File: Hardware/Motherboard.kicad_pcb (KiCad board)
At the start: 2 copper layers, 11 parts, among them J1 Pin_Header_02x08, J2 Pin_Header_02x08, J3 Pin_Header_02x08, U1 PIC18F26K22-I-SO, U2 FT240XS, U3 TXB0104D, U4 TXB0104D

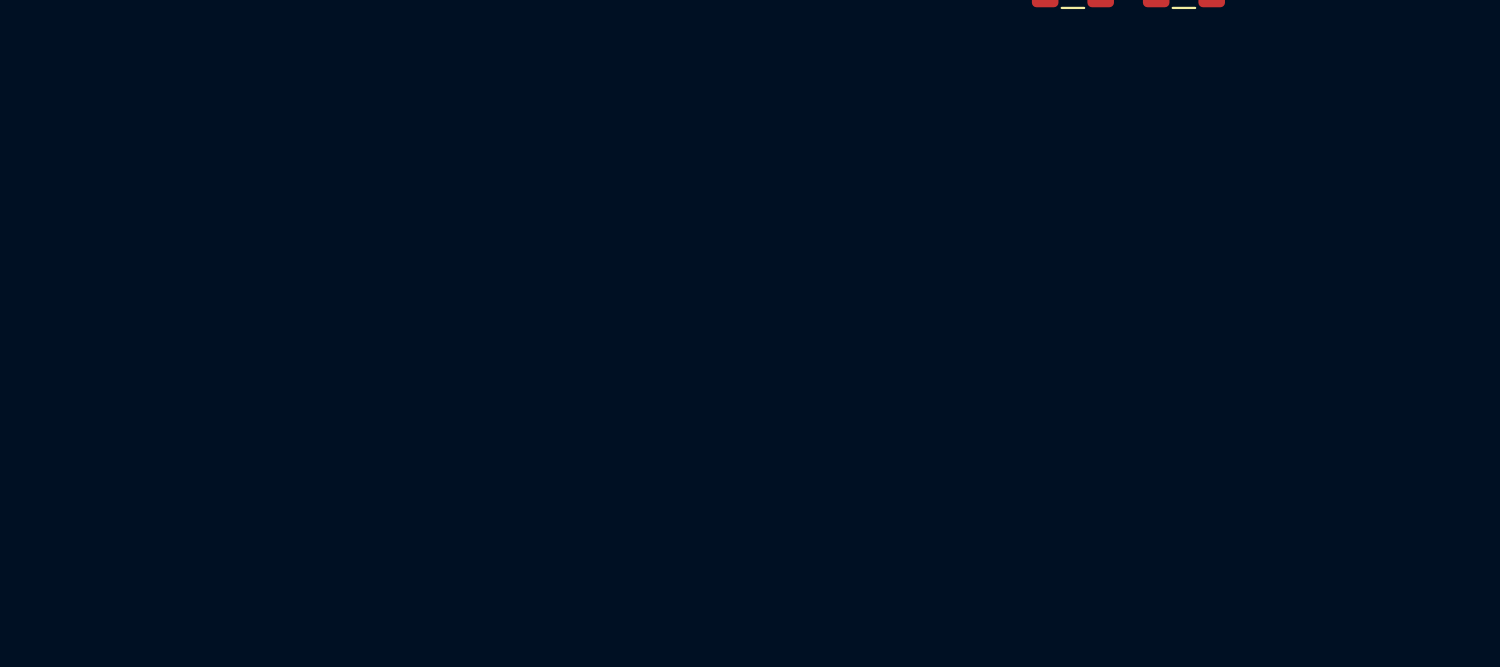
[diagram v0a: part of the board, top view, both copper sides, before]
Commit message: [Hardware] Added FTDI FIFO and logic signals output voltage switch to schematic.
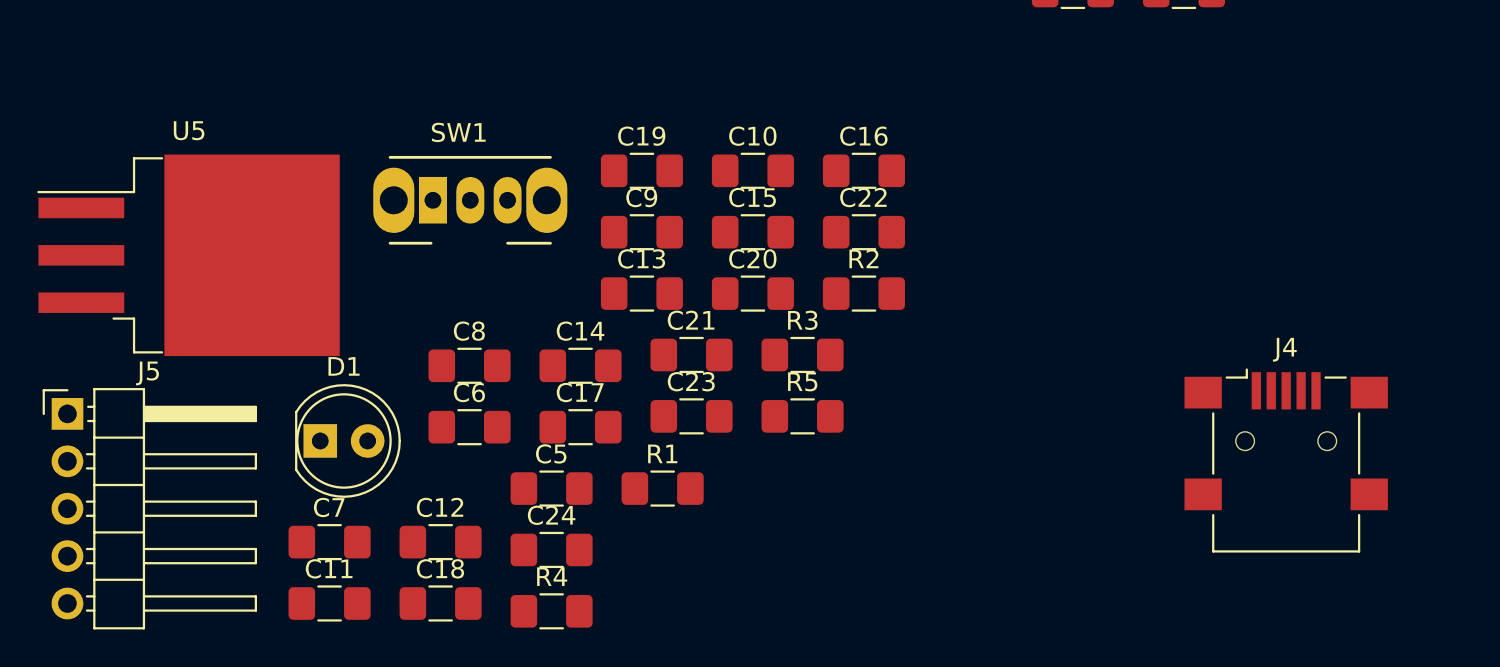
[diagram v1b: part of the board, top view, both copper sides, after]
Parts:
- added C10: 2.2u, Capacitor_SMD:C_1206_3216Metric_Pad1.42x1.75mm_HandSolder, F.Cu at (109.8, 74.4)
- added C11: 2.2u, Capacitor_SMD:C_1206_3216Metric_Pad1.42x1.75mm_HandSolder, F.Cu at (87.2, 97.6)
- added C12: 2.2u, Capacitor_SMD:C_1206_3216Metric_Pad1.42x1.75mm_HandSolder, F.Cu at (93.1, 94.3)
- added C13: 100n, Capacitor_SMD:C_1206_3216Metric_Pad1.42x1.75mm_HandSolder, F.Cu at (103.9, 81.0)
- added C14: 100n, Capacitor_SMD:C_1206_3216Metric_Pad1.42x1.75mm_HandSolder, F.Cu at (100.6, 84.9)
- added C15: 47p, Capacitor_SMD:C_1206_3216Metric_Pad1.42x1.75mm_HandSolder, F.Cu at (109.8, 77.7)
- added C16: 47p, Capacitor_SMD:C_1206_3216Metric_Pad1.42x1.75mm_HandSolder, F.Cu at (115.8, 74.4)
- added C17: 100n, Capacitor_SMD:C_1206_3216Metric_Pad1.42x1.75mm_HandSolder, F.Cu at (100.6, 88.2)
- added C18: 2.2u, Capacitor_SMD:C_1206_3216Metric_Pad1.42x1.75mm_HandSolder, F.Cu at (93.1, 97.6)
- added C19: 100n, Capacitor_SMD:C_1206_3216Metric_Pad1.42x1.75mm_HandSolder, F.Cu at (103.9, 74.4)
- added C20: 100n, Capacitor_SMD:C_1206_3216Metric_Pad1.42x1.75mm_HandSolder, F.Cu at (109.8, 81.0)
- added C21: 2.2u, Capacitor_SMD:C_1206_3216Metric_Pad1.42x1.75mm_HandSolder, F.Cu at (106.6, 84.3)
- added C22: 2.2u, Capacitor_SMD:C_1206_3216Metric_Pad1.42x1.75mm_HandSolder, F.Cu at (115.8, 77.7)
- added C23: 2.2u, Capacitor_SMD:C_1206_3216Metric_Pad1.42x1.75mm_HandSolder, F.Cu at (106.6, 87.6)
- added C24: 2.2u, Capacitor_SMD:C_1206_3216Metric_Pad1.42x1.75mm_HandSolder, F.Cu at (99.1, 94.7)
- added C5: 100n, Capacitor_SMD:C_1206_3216Metric_Pad1.42x1.75mm_HandSolder, F.Cu at (99.1, 91.4)
- added C6: 100n, Capacitor_SMD:C_1206_3216Metric_Pad1.42x1.75mm_HandSolder, F.Cu at (94.7, 88.2)
- added C7: 100n, Capacitor_SMD:C_1206_3216Metric_Pad1.42x1.75mm_HandSolder, F.Cu at (87.2, 94.3)
- added C8: 100n, Capacitor_SMD:C_1206_3216Metric_Pad1.42x1.75mm_HandSolder, F.Cu at (94.7, 84.9)
- added C9: 2.2u, Capacitor_SMD:C_1206_3216Metric_Pad1.42x1.75mm_HandSolder, F.Cu at (103.9, 77.7)
- added D1: LED, LED_THT:LED_D5.0mm, F.Cu at (86.7, 88.9)
- added J4: USB_B_Mini, Connector_USB:USB_Mini-B_Lumberg_2486_01_Horizontal, F.Cu at (138.4, 88.9)
- added J5: JTAG, Connector_PinHeader_2.54mm:PinHeader_1x05_P2.54mm_Horizontal, F.Cu at (73.1, 87.4)
- added R1: 82, Resistor_SMD:R_1206_3216Metric_Pad1.42x1.75mm_HandSolder, F.Cu at (105.0, 91.4)
- added R2: 27, Resistor_SMD:R_1206_3216Metric_Pad1.42x1.75mm_HandSolder, F.Cu at (115.8, 81.0)
- added R3: 27, Resistor_SMD:R_1206_3216Metric_Pad1.42x1.75mm_HandSolder, F.Cu at (112.5, 84.3)
- added R4: 10K, Resistor_SMD:R_1206_3216Metric_Pad1.42x1.75mm_HandSolder, F.Cu at (99.1, 98.0)
- added R5: 220, Resistor_SMD:R_1206_3216Metric_Pad1.42x1.75mm_HandSolder, F.Cu at (112.5, 87.6)
- added SW1: SW_SPDT, Button_Switch_THT:SW_CuK_OS102011MA1QN1_SPDT_Angled, F.Cu at (92.7, 76.0)
- added U5: MCP1826S, Package_TO_SOT_SMD:TO-263-3_TabPin2, F.Cu at (79.6, 78.9)
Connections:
- C3 pad 1: Net-(C3-Pad1) -> /TRANSLATOR_VCC
- C4 pad 1: Net-(C4-Pad1) -> /TRANSLATOR_VCC
- U1 pad 20: Net-(U1-Pad20) -> +3V3
- U1 pad 21: Net-(U1-Pad21) -> /FTDI_RXF
- U1 pad 22: Net-(U1-Pad22) -> /FTDI_TXE
- U1 pad 23: Net-(U1-Pad23) -> /FTDI_RD
- U1 pad 24: Net-(U1-Pad24) -> /FTDI_WR
- U1 pad 25: Net-(U1-Pad25) -> /FTDI_SIWU
- U2 pad 10: Net-(U2-Pad10) -> /FTDI_SIWU
- U2 pad 11: Net-(U2-Pad11) -> /FTDI_RD
- U2 pad 12: Net-(U2-Pad12) -> /FTDI_WR
- U2 pad 15: Net-(U2-Pad15) -> +3.3VA
- U2 pad 16: Net-(U2-Pad16) -> +3.3VA
- U2 pad 18: Net-(U2-Pad18) -> +5V
- U2 pad 20: Net-(U2-Pad20) -> /FTDI_TXE
- U2 pad 21: Net-(U2-Pad21) -> /FTDI_RXF
- U2 pad 3: Net-(U2-Pad3) -> +3.3VA
- U3 pad 14: Net-(C3-Pad1) -> /TRANSLATOR_VCC
- U4 pad 14: Net-(C4-Pad1) -> /TRANSLATOR_VCC

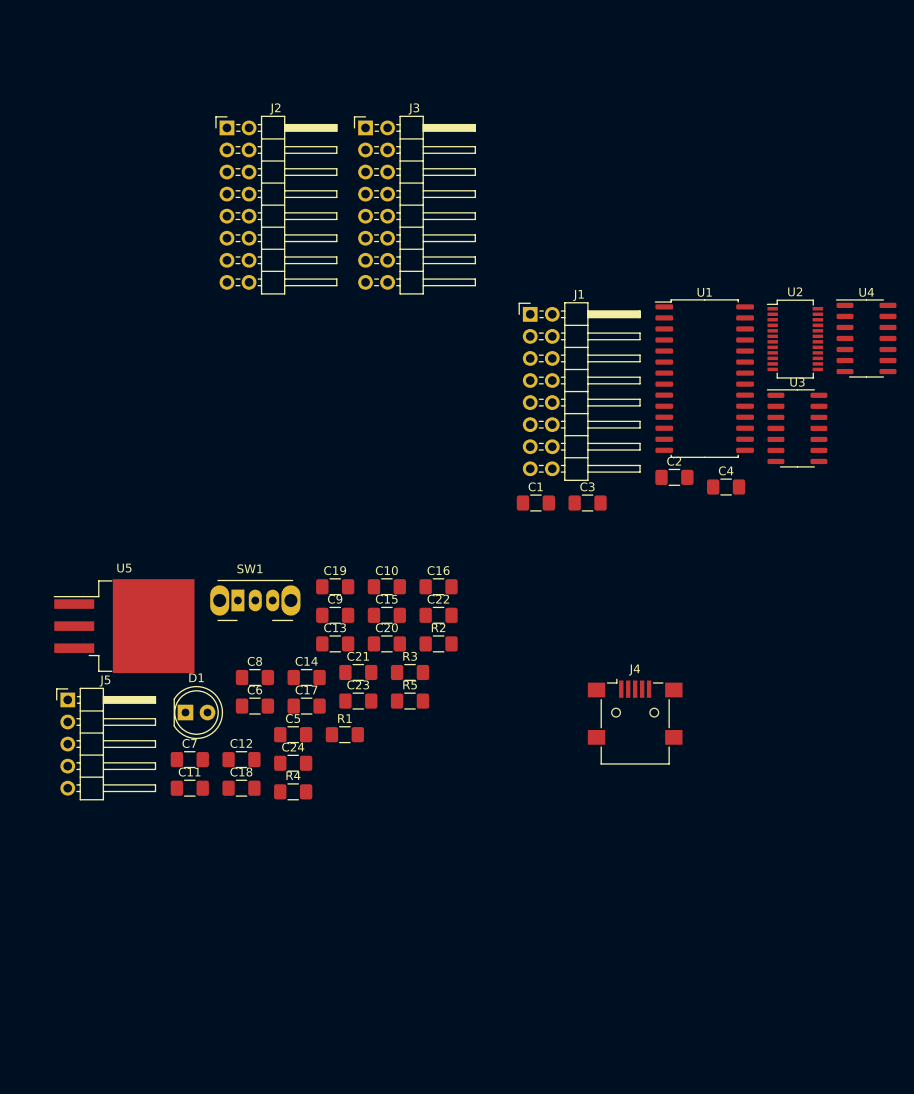
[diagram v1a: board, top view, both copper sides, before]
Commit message: [Hardware] Placed components on PCB.
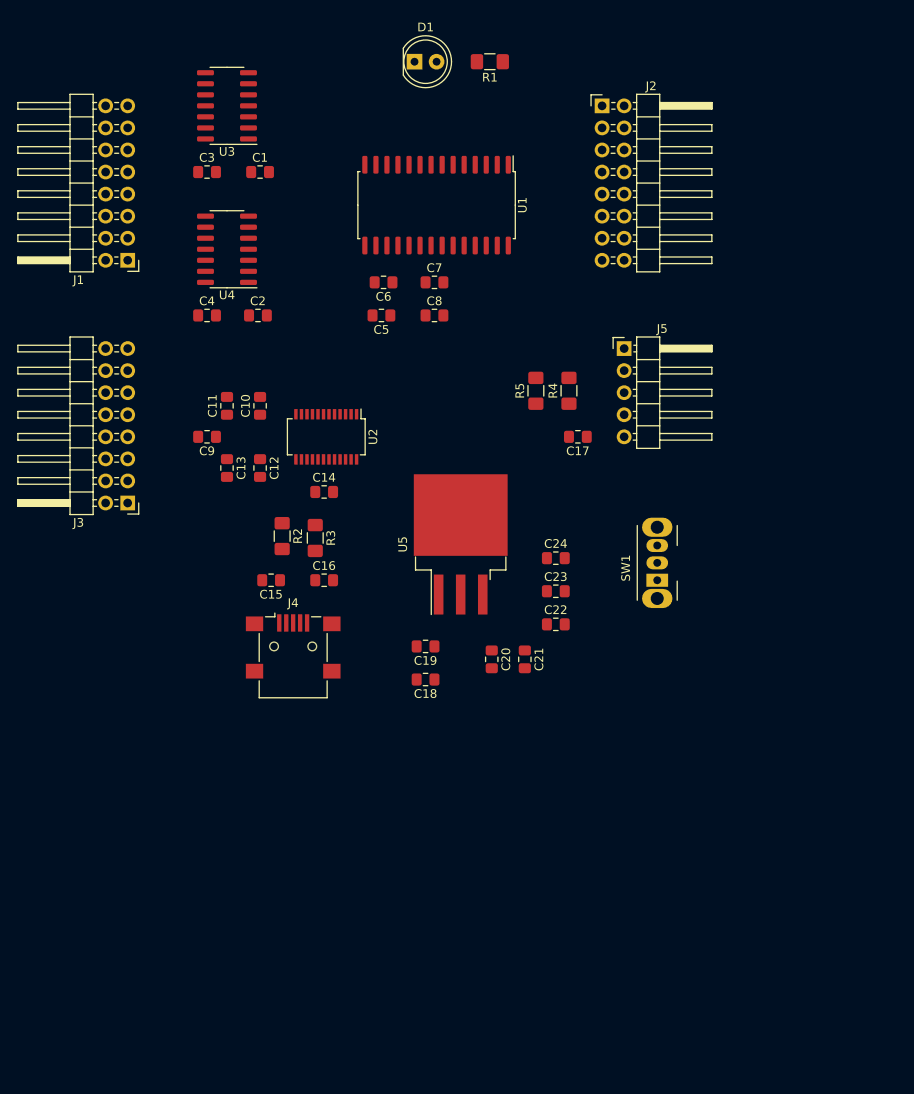
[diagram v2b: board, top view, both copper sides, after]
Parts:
- C1, C10, C11, C12, C13, C14, C15, C16, C17, C18, C19, C2, C20, C21, C22, C23, C24, C3, C4, C5, C6, C7, C8, C9: footprint Capacitor_SMD:C_1206_3216Metric_Pad1.42x1.75mm_HandSolder -> Capacitor_SMD:C_0805_2012Metric_Pad1.15x1.40mm_HandSolder
- moved D1 79.4 mm to (113.0, 14.0)
- moved R1 79.2 mm to (121.7, 14.0), turned to 180 degrees
- moved J5 75.8 mm to (137.2, 47.0)
- moved U3 75.4 mm to (91.4, 19.1), turned to 180 degrees
- moved U4 74.3 mm to (91.4, 35.6), turned to 180 degrees
- moved C4 62.9 mm to (89.1, 43.2)
- moved C7 61.7 mm to (115.3, 39.4)
- moved C3 58.1 mm to (89.1, 26.7)
- moved R4 56.0 mm to (130.8, 51.9), turned to 90 degrees
- moved U2 55.1 mm to (102.9, 57.1), turned to 270 degrees
- moved C2 51.4 mm to (95.0, 43.2)
- moved J3 51.1 mm to (80.0, 64.8), turned to 180 degrees
- moved C6 51.0 mm to (109.5, 39.4), turned to 180 degrees
- moved C1 49.6 mm to (95.2, 26.7)
- moved C5 49.3 mm to (109.2, 43.2), turned to 180 degrees
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
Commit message: [Hardware] Added PCB mounting holes.
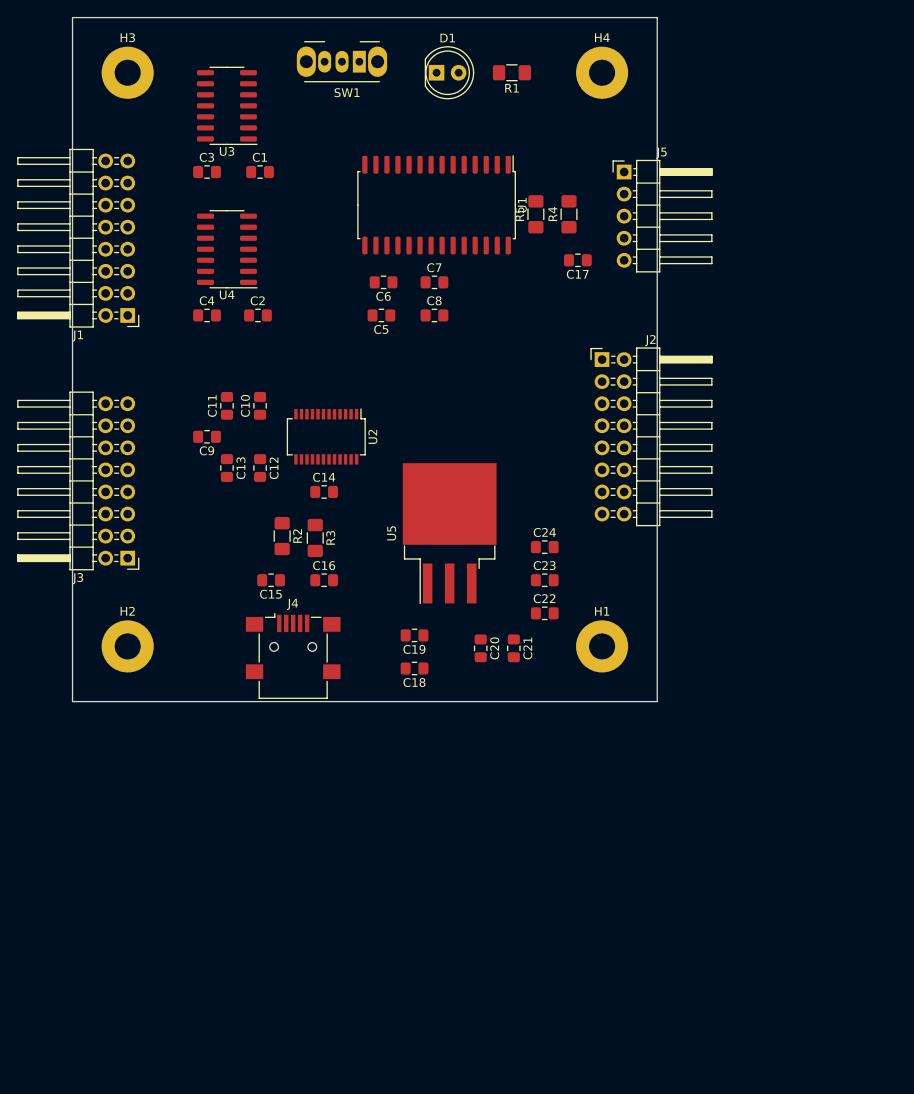
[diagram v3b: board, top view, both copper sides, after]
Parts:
- added H1: Hole, MountingHole:MountingHole_3mm_Pad, F.Cu at (134.6, 81.3)
- added H2: Hole, MountingHole:MountingHole_3mm_Pad, F.Cu at (80.0, 81.3)
- added H3: Hole, MountingHole:MountingHole_3mm_Pad, F.Cu at (80.0, 15.2)
- added H4: Hole, MountingHole:MountingHole_3mm_Pad, F.Cu at (134.6, 15.2)
- moved SW1 68.8 mm to (106.7, 14.0), turned to 180 degrees
- moved J2 29.2 mm to (134.6, 48.3)
- moved C17 20.3 mm to (131.8, 36.8)
- moved J5 20.3 mm to (137.2, 26.7)
- moved R4 20.3 mm to (130.8, 31.5)
- moved R5 20.3 mm to (127.0, 31.5)
- moved J3 6.35 mm to (80.0, 71.1)
- moved J1 6.35 mm to (80.0, 43.2)
- moved R1 2.84 mm to (124.2, 15.2)
- moved D1 2.84 mm to (115.6, 15.2)
- moved C18 1.80 mm to (113.0, 83.8)
- moved C21 1.80 mm to (124.5, 81.5)
- moved C19 1.80 mm to (113.0, 80.0)
- moved C20 1.80 mm to (120.7, 81.5)
- moved U5 1.80 mm to (117.1, 68.3)
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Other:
- board outline added: 67.3 x 78.7 mm

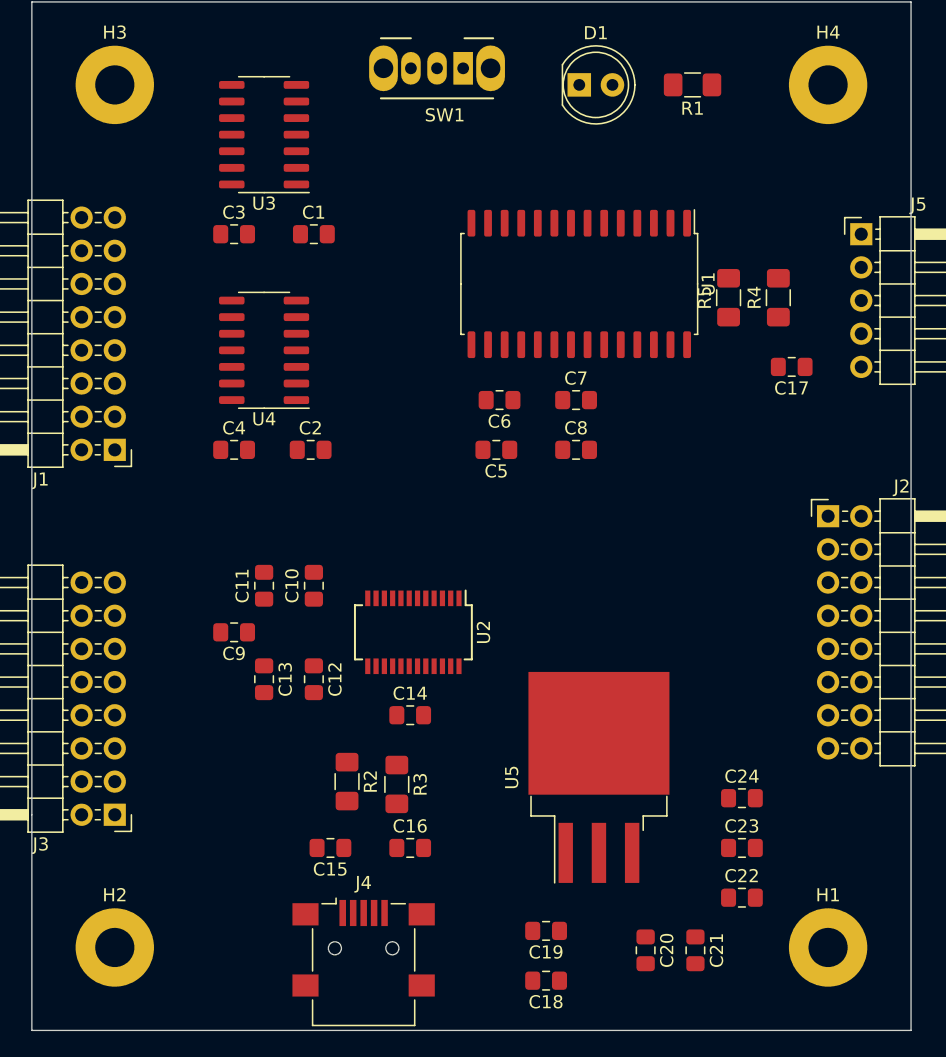
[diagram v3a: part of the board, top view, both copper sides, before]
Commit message: [Hardware] Started PCB routing. Switched to 4 layers to have power supply planes.
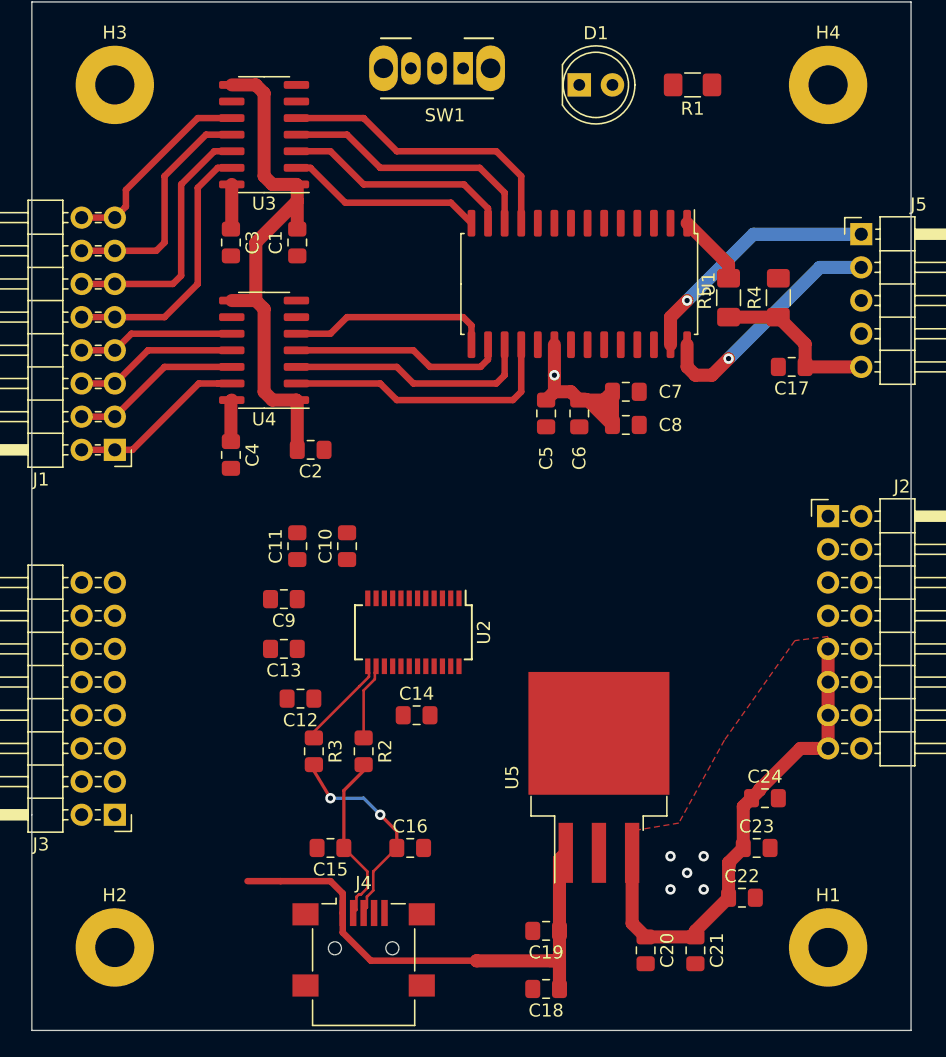
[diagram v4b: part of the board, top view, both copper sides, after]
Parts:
- R2, R3: footprint Resistor_SMD:R_1206_3216Metric_Pad1.42x1.75mm_HandSolder -> Resistor_SMD:R_0805_2012Metric_Pad1.15x1.40mm_HandSolder
- moved R3 6.84 mm to (95.2, 66.3)
- moved C6 6.19 mm to (115.6, 40.4), turned to 270 degrees
- moved C5 4.72 mm to (113.0, 40.4), turned to 270 degrees
- moved C9 4.58 mm to (93.0, 54.6)
- moved C8 4.26 mm to (119.1, 41.3)
- moved C10 3.95 mm to (97.8, 50.6)
- moved C11 3.95 mm to (94.0, 50.6)
- moved C7 3.86 mm to (119.1, 38.7)
- moved C13 2.77 mm to (93.0, 58.4), turned to 180 degrees
- moved R2 2.65 mm to (99.1, 66.3)
- moved C12 1.81 mm to (94.2, 62.2), turned to 180 degrees
- moved C24 1.76 mm to (129.8, 69.8)
- moved C1 1.42 mm to (94.0, 27.3), turned to 90 degrees
- moved C23 1.12 mm to (129.2, 73.7)
- moved C3 0.68 mm to (88.9, 27.3), turned to 270 degrees
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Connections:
- net Net-(C15-Pad1) renamed /USB_1_D-
- net Net-(C16-Pad1) renamed /USB_1_D+
- net Net-(R2-Pad1) renamed /USB_2_D+
- net Net-(R3-Pad1) renamed /USB_2_D-
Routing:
- net +3V3: track 0.00 -> 94.3 mm, vias 0 -> 6
- net +5V: track 0.00 -> 46.7 mm
- net Net-(U1-Pad11): track 0.00 -> 22.7 mm
- net Net-(U1-Pad18): track 0.00 -> 21.6 mm
- net Net-(J1-Pad10): track 0.00 -> 20.5 mm
- net Net-(U1-Pad12): track 0.00 -> 20.1 mm
- net Net-(J1-Pad11): track 0.00 -> 19.8 mm
- net Net-(J5-Pad1): track 0.00 -> 19.3 mm, vias 0 -> 1
- net Net-(U1-Pad17): track 0.00 -> 19.1 mm
- net Net-(J5-Pad2): track 0.00 -> 18.7 mm, vias 0 -> 1
- net Net-(J1-Pad13): track 0.00 -> 18.2 mm
- net Net-(U1-Pad13): track 0.00 -> 17.6 mm
- net Net-(U1-Pad16): track 0.00 -> 16.6 mm
- net /USB_1_D+: track 0.00 -> 15.9 mm, vias 0 -> 2
- net Net-(U1-Pad15): track 0.00 -> 15.7 mm
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- added copper zone on F.Cu, net +3V3
- added copper zone on In1.Cu, net +3V3
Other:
- copper layers 2 -> 4
- net class Power added: clearance 0.2, trace_width 1, via_dia 0.8, via_drill 0.4
